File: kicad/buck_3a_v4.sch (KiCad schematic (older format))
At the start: 25 parts, among them J1 LED+, J2 LED-, J3 Conn_01x04, J4 Conn_01x02, J5 Conn_01x06, Q1 BSC042NE78NS36, U1 MAX16819ATT+T, U2 ATtiny45-20SU

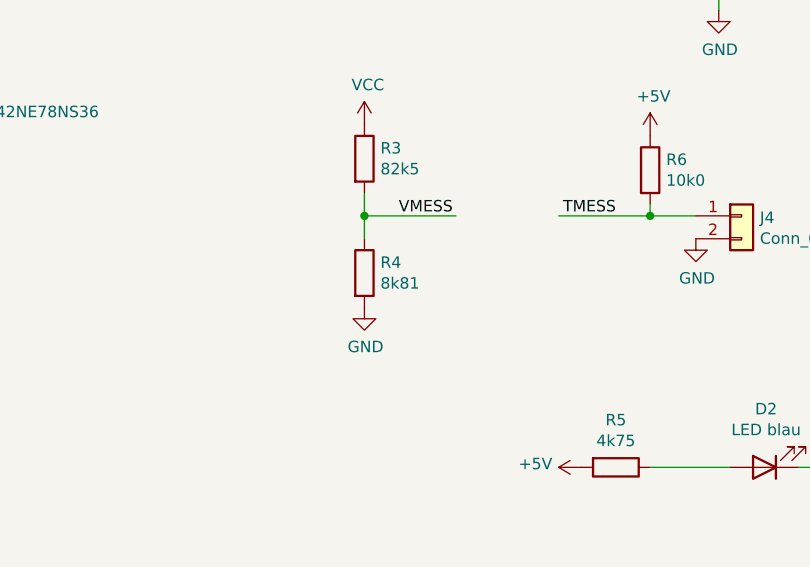
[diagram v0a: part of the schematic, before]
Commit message: uc_src angepasst
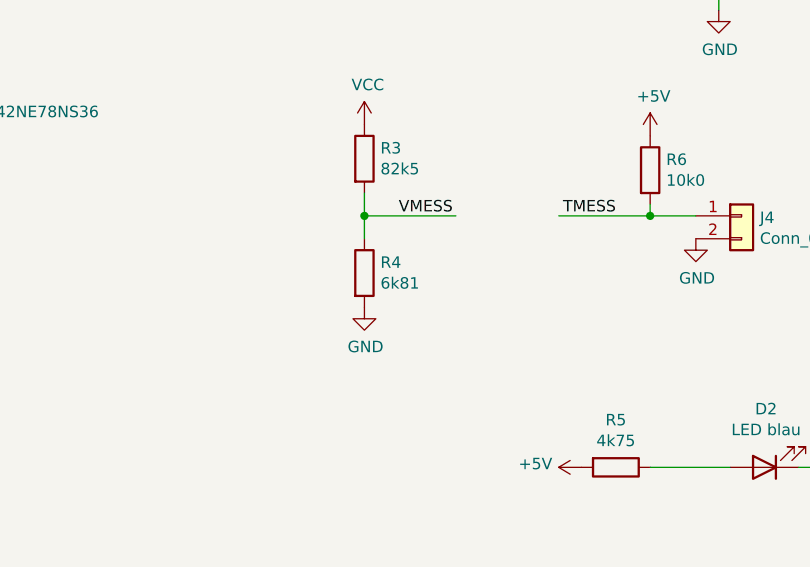
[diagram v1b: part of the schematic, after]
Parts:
- R4: value 8k81 -> 6k81
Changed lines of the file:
@@
 P 6800 4550
 F 0 "R4" H 6870 4596 50  0000 L CNN
-F 1 "8k81" H 6870 4505 50  0000 L CNN
+F 1 "6k81" H 6870 4505 50  0000 L CNN
 F 2 "Resistor_SMD:R_0805_2012Metric" V 6730 4550 50  0001 C CNN
 F 3 "~" H 6800 4550 50  0001 C CNN

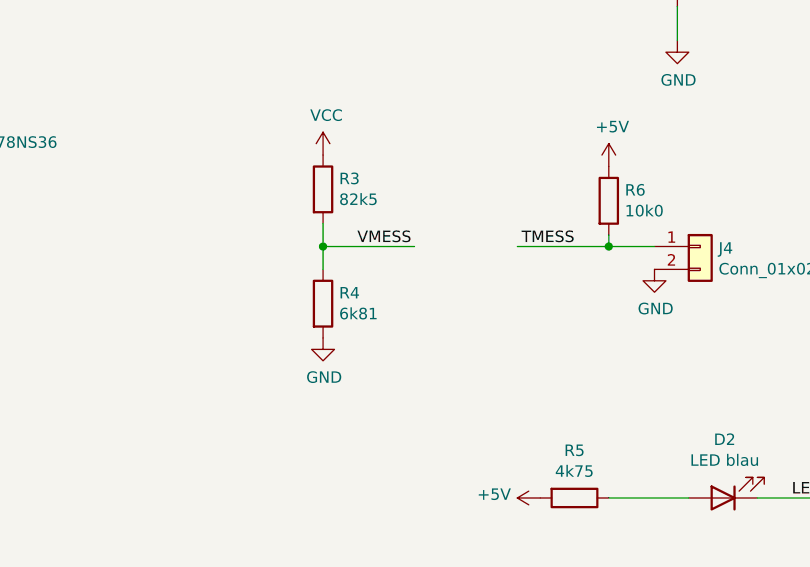
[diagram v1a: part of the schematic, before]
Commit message: change some parts to non-china parts add some gnd vias to JST connector add new chapter to Aufbau.pdf port uc firmware to new Uc
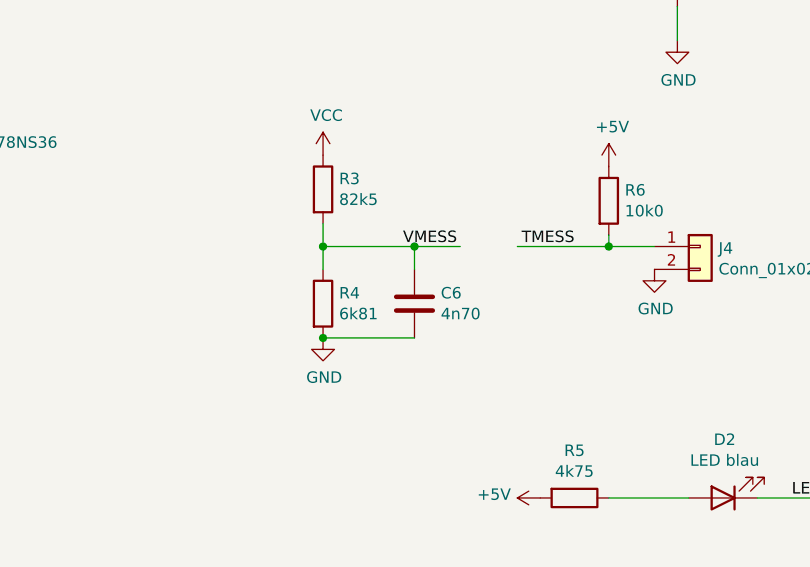
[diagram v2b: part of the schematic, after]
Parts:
- added C6: 4n70, Capacitor_SMD:C_0805_2012Metric, symbol Device:C
- D1: footprint Diode_SMD:D_SMA -> Diode_SMD:D_PowerDI-5
- L1: footprint Inductor_SMD:L_6.3x6.3_H3 -> Inductor_SMD:L_10.4x10.4_H4.8
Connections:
- wire segments 64 -> 67
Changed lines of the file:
@@
 F 0 "L1" V 4540 2600 50  0000 C CNN
 F 1 "MWSA0603-100MT" V 4449 2600 50  0000 C CNN
-F 2 "Inductor_SMD:L_6.3x6.3_H3" H 4350 2600 50  0001 C CNN
+F 2 "Inductor_SMD:L_10.4x10.4_H4.8" H 4350 2600 50  0001 C CNN
 F 3 "~" H 4350 2600 50  0001 C CNN
 F 4 "C132141" V 4350 2600 50  0001 C CNN "LCSC"
@@
 F 0 "D1" H 3400 2467 50  0000 C CNN
 F 1 "SS54" H 3400 2376 50  0000 C CNN
-F 2 "Diode_SMD:D_SMA" H 3400 2250 50  0001 C CNN
+F 2 "Diode_SMD:D_PowerDI-5" H 3400 2250 50  0001 C CNN
 F 3 "~" H 3400 2250 50  0001 C CNN
 F 4 "C22452" H 3400 2250 50  0001 C CNN "LCSC"
@@
 Text Label 9250 2550 0    50   ~ 0
 MODE
-Wire Wire Line
-	6800 4200 6800 4300
-Wire Wire Line
-	6800 4300 7200 4300
-Connection ~ 6800 4300
-Wire Wire Line
-	6800 4300 6800 4400
-Text Label 6950 4300 0    50   ~ 0
+Text Label 7150 4300 0    50   ~ 0
 VMESS
 $Comp
@@
 	1    0    0    -1
 $EndComp
+Connection ~ 6800 4300
+Wire Wire Line
+	6800 4300 6800 4400
+Wire Wire Line
+	6800 4200 6800 4300
+Wire Wire Line
+	6800 4300 7200 4300
+$Comp
+L Device:C C6
+U 1 1 5FB6DC72
+P 7200 4550
+F 0 "C6" H 7315 4596 50  0000 L CNN
+F 1 "4n70" H 7315 4505 50  0000 L CNN
+F 2 "Capacitor_SMD:C_0805_2012Metric" H 7238 4400 50  0001 C CNN
+F 3 "~" H 7200 4550 50  0001 C CNN
+	1    7200 4550
+	1    0    0    -1
+$EndComp
+Wire Wire Line
+	7200 4400 7200 4300
+Connection ~ 7200 4300
+Wire Wire Line
+	7200 4300 7400 4300
+Wire Wire Line
+	7200 4700 6800 4700
+Connection ~ 6800 4700
 $EndSCHEMATC

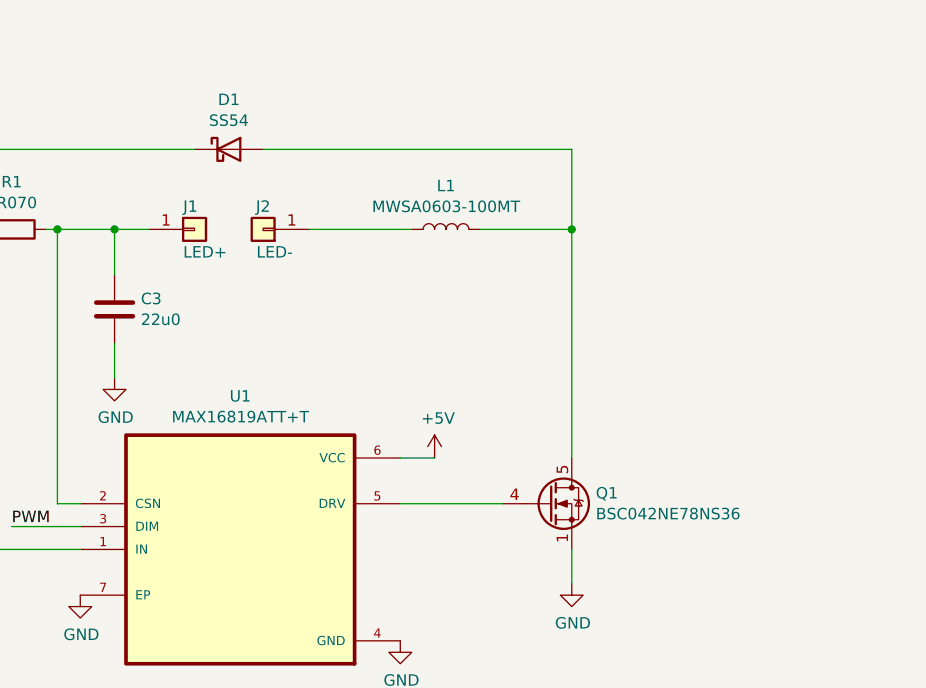
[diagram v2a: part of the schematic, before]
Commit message: Fix sleep mode with battery pack
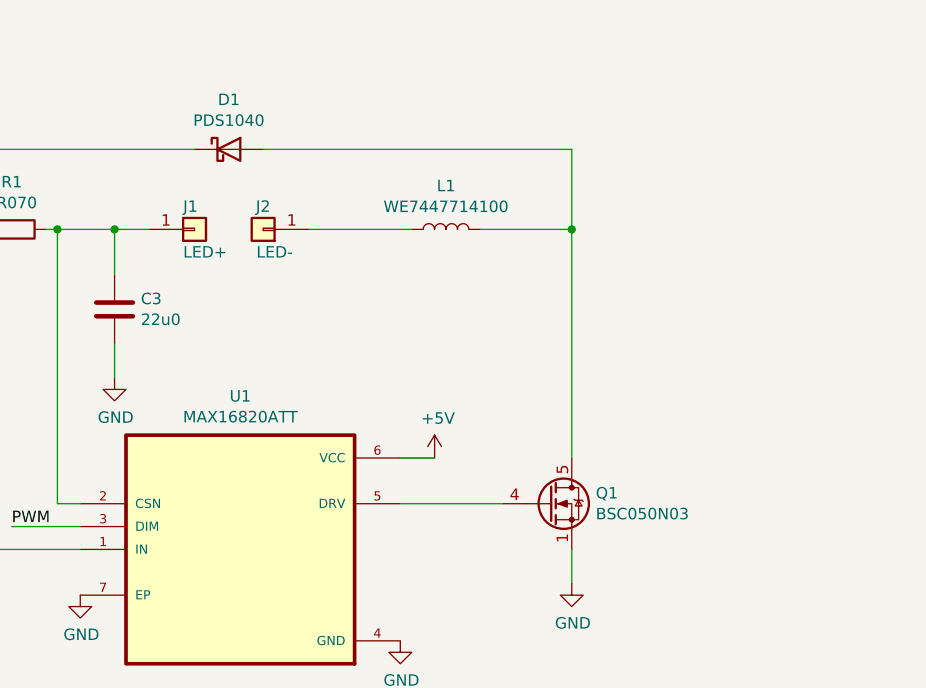
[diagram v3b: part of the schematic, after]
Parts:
- D1: value SS54 -> PDS1040
- L1: value MWSA0603-100MT -> WE7447714100
- Q1: value BSC042NE78NS36 -> BSC050N03
- U1: value MAX16819ATT+T -> MAX16820ATT
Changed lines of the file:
@@
 P 3450 4000
 F 0 "U1" H 3450 4670 50  0000 C CNN
-F 1 "MAX16819ATT+T" H 3450 4579 50  0000 C CNN
+F 1 "MAX16820ATT" H 3450 4579 50  0000 C CNN
 F 2 "buck_3a_v4:SON95P300X300X80-7N" H 3450 4000 50  0001 L BNN
 F 3 "" H 3450 4000 50  0001 C CNN
@@
 P 4350 2600
 F 0 "L1" V 4540 2600 50  0000 C CNN
-F 1 "MWSA0603-100MT" V 4449 2600 50  0000 C CNN
+F 1 "WE7447714100" V 4449 2600 50  0000 C CNN
 F 2 "Inductor_SMD:L_10.4x10.4_H4.8" H 4350 2600 50  0001 C CNN
 F 3 "~" H 4350 2600 50  0001 C CNN
@@
 P 4800 3800
 F 0 "Q1" H 5005 3846 50  0000 L CNN
-F 1 "BSC042NE78NS36" H 5005 3755 50  0000 L CNN
+F 1 "BSC050N03" H 5005 3755 50  0000 L CNN
 F 2 "Package_TO_SOT_SMD:TDSON-8-1" H 5000 3725 50  0001 L CIN
 F 3 "http://www.infineon.com/dgdl/Infineon-BSC040N08NS5-DS-v02_00-EN.pdf?fileId=5546d4624ad04ef9014ae3065a7e2a05" V 4800 3800 50  0001 L CNN
@@
 P 3400 2250
 F 0 "D1" H 3400 2467 50  0000 C CNN
-F 1 "SS54" H 3400 2376 50  0000 C CNN
+F 1 "PDS1040" H 3400 2376 50  0000 C CNN
 F 2 "Diode_SMD:D_PowerDI-5" H 3400 2250 50  0001 C CNN
 F 3 "~" H 3400 2250 50  0001 C CNN

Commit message: save
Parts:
- C1, C3: value 22u0 -> 100u/16V; footprint Capacitor_SMD:C_0805_2012Metric -> Capacitor_SMD:C_1210_3225Metric
- C4: value 22u0 -> 47u0; footprint Capacitor_SMD:C_0805_2012Metric -> Capacitor_SMD:C_1206_3216Metric
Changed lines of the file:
@@
 P 6600 2600
 F 0 "C4" H 6715 2646 50  0000 L CNN
-F 1 "22u0" H 6715 2555 50  0000 L CNN
-F 2 "Capacitor_SMD:C_0805_2012Metric" H 6638 2450 50  0001 C CNN
+F 1 "47u0" H 6715 2555 50  0000 L CNN
+F 2 "Capacitor_SMD:C_1206_3216Metric" H 6638 2450 50  0001 C CNN
 F 3 "~" H 6600 2600 50  0001 C CNN
 F 4 "C45783" H 6600 2600 50  0001 C CNN "LCSC"
@@
 P 2900 2950
 F 0 "C3" H 3015 2996 50  0000 L CNN
-F 1 "22u0" H 3015 2905 50  0000 L CNN
-F 2 "Capacitor_SMD:C_0805_2012Metric" H 2938 2800 50  0001 C CNN
+F 1 "100u/16V" H 3015 2905 50  0000 L CNN
+F 2 "Capacitor_SMD:C_1210_3225Metric" H 2938 2800 50  0001 C CNN
 F 3 "~" H 2900 2950 50  0001 C CNN
 F 4 "C45783" H 2900 2950 50  0001 C CNN "LCSC"
@@
 P 1350 2950
 F 0 "C1" H 1465 2996 50  0000 L CNN
-F 1 "22u0" H 1465 2905 50  0000 L CNN
-F 2 "Capacitor_SMD:C_0805_2012Metric" H 1388 2800 50  0001 C CNN
+F 1 "100u/16V" H 1465 2905 50  0000 L CNN
+F 2 "Capacitor_SMD:C_1210_3225Metric" H 1388 2800 50  0001 C CNN
 F 3 "~" H 1350 2950 50  0001 C CNN
 F 4 "C45783" H 1350 2950 50  0001 C CNN "LCSC"
